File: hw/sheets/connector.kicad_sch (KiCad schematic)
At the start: 1 part, among them J1 AH58893-T9B10-3F

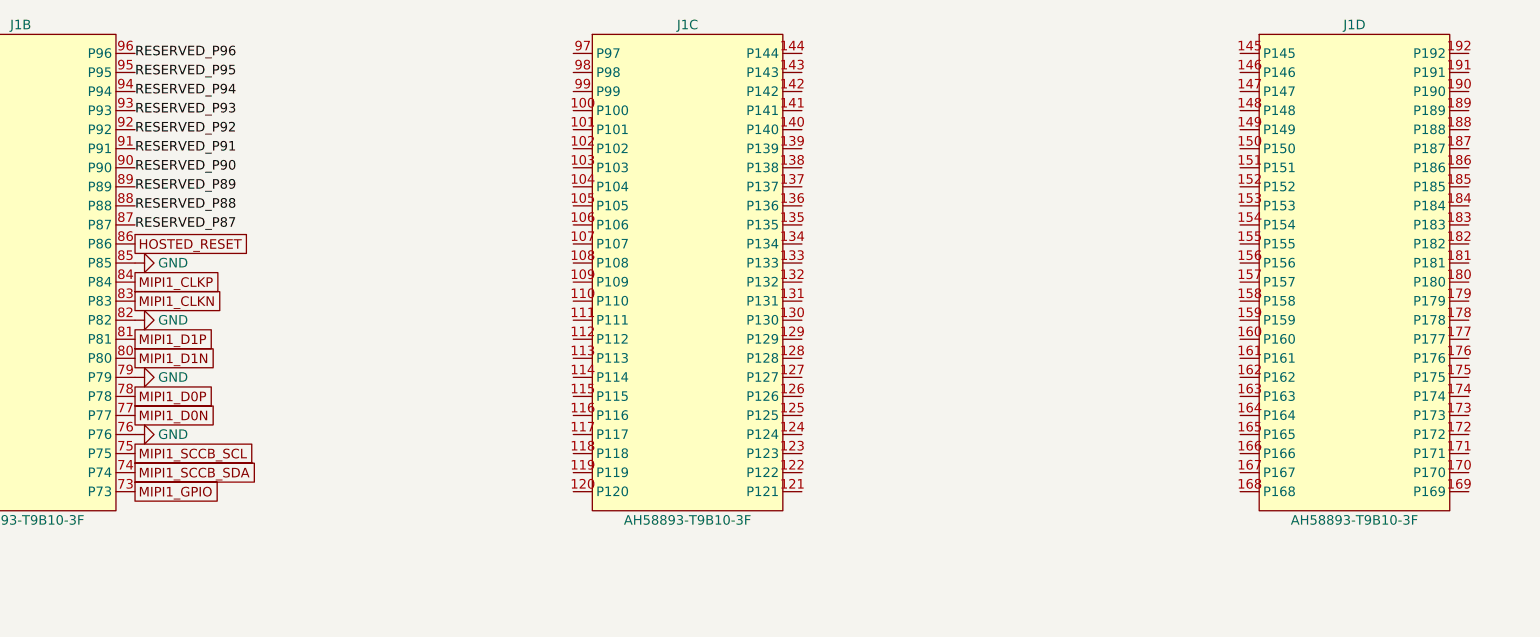
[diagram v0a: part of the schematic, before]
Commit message: Carrier board: pin-breakout header sheet (SS8 superset)
Assigns J1 pins 87-169 (previously RESERVED_P87-96 and unconnected)
to the per-SoC GPIO/peripheral superset and breaks them out onto 11
function-clustered, labeled 0.1" headers on a new headers.kicad_sch
sheet: GMAC0/GMAC1 (RGMII, A1's real 2nd MAC), UART0/UART2/UART3
(no UART4/UART5 -- verified no T-series/A1 SoC has them), SSI0, SSI1,
PWM0-7, SAR-ADC, general SMB0/SMB1 (isolated from the carrier-ID I2C
bus), and 16 plain GPIO. Clustering is a silkscreen convenience only,
not an electrical constraint.

Verified: 0 layout overlaps, netlist diff shows only J1 pins 87-169
and the new header refs changed, ERC errors went down (231->158,
purely fewer not-connected pins) with no new violation classes.

Also commits the schematic generator toolchain (hw/scripts/) that
built this and the previously-merged power/connector/bmc/io sections,
so the schematic has a reproducible source instead of only generated
output.
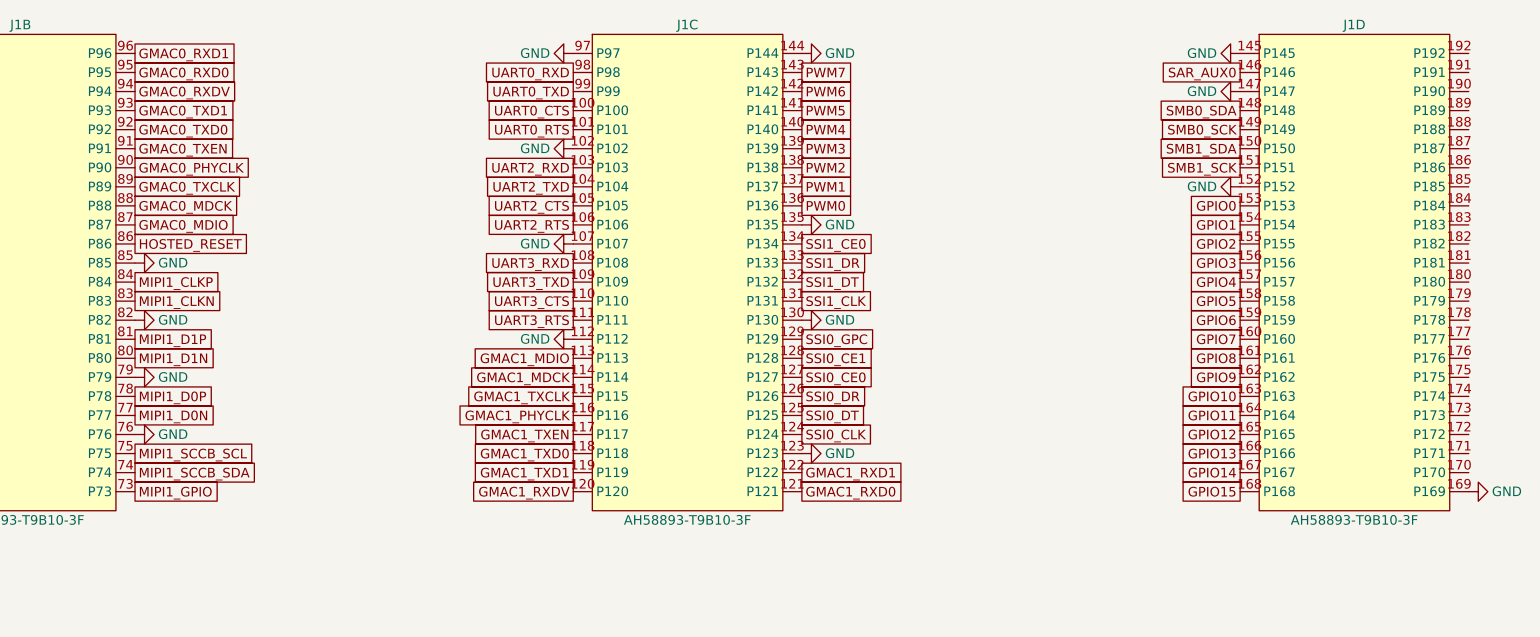
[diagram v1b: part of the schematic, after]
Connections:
- net GND: now also J1.102 (P102), J1.107 (P107), J1.112 (P112), J1.123 (P123), J1.130 (P130), J1.135 (P135), J1.144 (P144), J1.145 (P145), J1.147 (P147), J1.152 (P152), J1.169 (P169), J1.97 (P97)
- net SAR_AUX0: now reaches J1.146 (P146)
- net SMB0_SDA: now reaches J1.148 (P148)
- net SMB0_SCK: now reaches J1.149 (P149)
- net SMB1_SDA: now reaches J1.150 (P150)
- net SMB1_SCK: now reaches J1.151 (P151)
- net GPIO0: now reaches J1.153 (P153)
- net GPIO1: now reaches J1.154 (P154)
- net GPIO2: now reaches J1.155 (P155)
- net GPIO3: now reaches J1.156 (P156)
- net GPIO4: now reaches J1.157 (P157)
- net GPIO5: now reaches J1.158 (P158)
- net GPIO6: now reaches J1.159 (P159)
- net GPIO7: now reaches J1.160 (P160)
- net GPIO8: now reaches J1.161 (P161)
- net GPIO9: now reaches J1.162 (P162)
- net GPIO10: now reaches J1.163 (P163)
- net GPIO11: now reaches J1.164 (P164)
- net GPIO12: now reaches J1.165 (P165)
- net GPIO13: now reaches J1.166 (P166)
- net GPIO14: now reaches J1.167 (P167)
- net GPIO15: now reaches J1.168 (P168)
- net UART0_CTS: now reaches J1.100 (P100)
- net UART0_RTS: now reaches J1.101 (P101)
- net UART2_RXD: now reaches J1.103 (P103)
- net UART2_TXD: now reaches J1.104 (P104)
- net UART2_CTS: now reaches J1.105 (P105)
- net UART2_RTS: now reaches J1.106 (P106)
- net UART3_RXD: now reaches J1.108 (P108)
- net UART3_TXD: now reaches J1.109 (P109)
- net UART3_CTS: now reaches J1.110 (P110)
- net UART3_RTS: now reaches J1.111 (P111)
- net GMAC1_MDIO: now reaches J1.113 (P113)
- net GMAC1_MDCK: now reaches J1.114 (P114)
- net GMAC1_TXCLK: now reaches J1.115 (P115)
- net GMAC1_PHYCLK: now reaches J1.116 (P116)
- net GMAC1_TXEN: now reaches J1.117 (P117)
- net GMAC1_TXD0: now reaches J1.118 (P118)
- net GMAC1_TXD1: now reaches J1.119 (P119)
- net GMAC1_RXDV: now reaches J1.120 (P120)
- net GMAC1_RXD0: now reaches J1.121 (P121)
- net GMAC1_RXD1: now reaches J1.122 (P122)
- net SSI0_CLK: now reaches J1.124 (P124)
- net SSI0_DT: now reaches J1.125 (P125)
- net SSI0_DR: now reaches J1.126 (P126)
- net SSI0_CE0: now reaches J1.127 (P127)
- net SSI0_CE1: now reaches J1.128 (P128)
- net SSI0_GPC: now reaches J1.129 (P129)
- net SSI1_CLK: now reaches J1.131 (P131)
- net SSI1_DT: now reaches J1.132 (P132)
- net SSI1_DR: now reaches J1.133 (P133)
- net SSI1_CE0: now reaches J1.134 (P134)
- net PWM0: now reaches J1.136 (P136)
- net PWM1: now reaches J1.137 (P137)
- net PWM2: now reaches J1.138 (P138)
- net PWM3: now reaches J1.139 (P139)
- net PWM4: now reaches J1.140 (P140)
- net PWM5: now reaches J1.141 (P141)
- net PWM6: now reaches J1.142 (P142)
- net PWM7: now reaches J1.143 (P143)
- net UART0_RXD: now reaches J1.98 (P98)
- net UART0_TXD: now reaches J1.99 (P99)
- net RESERVED_P87 renamed GMAC0_MDIO
- net RESERVED_P88 renamed GMAC0_MDCK
- net RESERVED_P89 renamed GMAC0_TXCLK
- net RESERVED_P90 renamed GMAC0_PHYCLK
- net RESERVED_P91 renamed GMAC0_TXEN
- net RESERVED_P92 renamed GMAC0_TXD0
- net RESERVED_P93 renamed GMAC0_TXD1
- net RESERVED_P94 renamed GMAC0_RXDV
- net RESERVED_P95 renamed GMAC0_RXD0
- net RESERVED_P96 renamed GMAC0_RXD1
